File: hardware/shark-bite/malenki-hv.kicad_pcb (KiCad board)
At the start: 2 copper layers, 56.9 x 61.3 mm, 92 parts, among them J1 Conn_01x02_Male-Connector, J2 Conn_01x08_Male, J3 Conn_01x02, J4 Conn_01x02_Male-Connector, J5 Conn_01x02_Male-Connector, J6 Conn_01x03_Pin, U1 GM7333, U10 IRFH7440TRPBF, U11 IRFH7440TRPBF, U12 IRFH7440TRPBF, U13 DRV8231DSGR, U14 DRV8231DSGR, U2 ATTiny1616-MNR, U3 A7105, U4 GD32E230G6U6TR, U5 FD6288Q, U6 AOZ1282CI, U7 IRFH7440TRPBF, U8 IRFH7440TRPBF, U9 IRFH7440TRPBF, Y1 16mhz Seiko Epson Q24FA20H005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

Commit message: Routed Without Debug
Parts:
- moved C20 0.90 mm to (130.2, 76.9)
- moved C3 0.70 mm to (113.1, 52.5)
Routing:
- net GND: track 380.8 -> 368.9 mm, vias 63 -> 57
- net VLOGIC: track 117.7 -> 127.2 mm
- net BEMF_A: track 12.5 -> 16.8 mm
- net TXDEBUG: track 37.2 -> 35.2 mm
- net Net-(U2-PA3): track 14.1 -> 15.8 mm
- net GATE_HIGH_B: track 27.5 -> 29.0 mm
- net OUT_B: track 70.3 -> 71.4 mm
- net OUT_A: track 73.0 -> 74.0 mm
- net VSENSE: track 10.7 -> 11.7 mm
- net GATE_HIGH_A: track 23.9 -> 24.5 mm, vias 5 -> 4
- net Net-(D5-K): track 14.3 -> 14.9 mm
- net GIO1: track 23.3 -> 23.9 mm
- net GATE_LOW_B: track 26.1 -> 26.6 mm

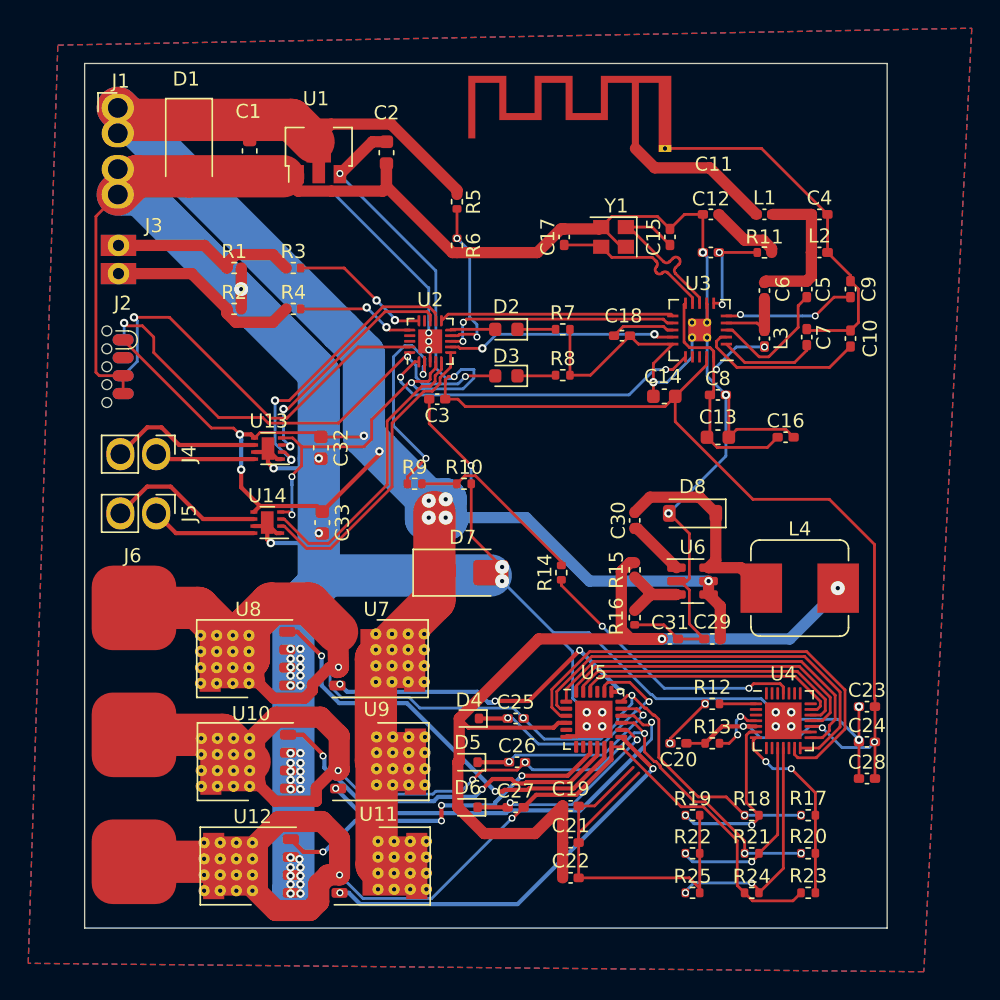
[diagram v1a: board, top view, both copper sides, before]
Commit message: Added Gate Resistors and Power Capacitors
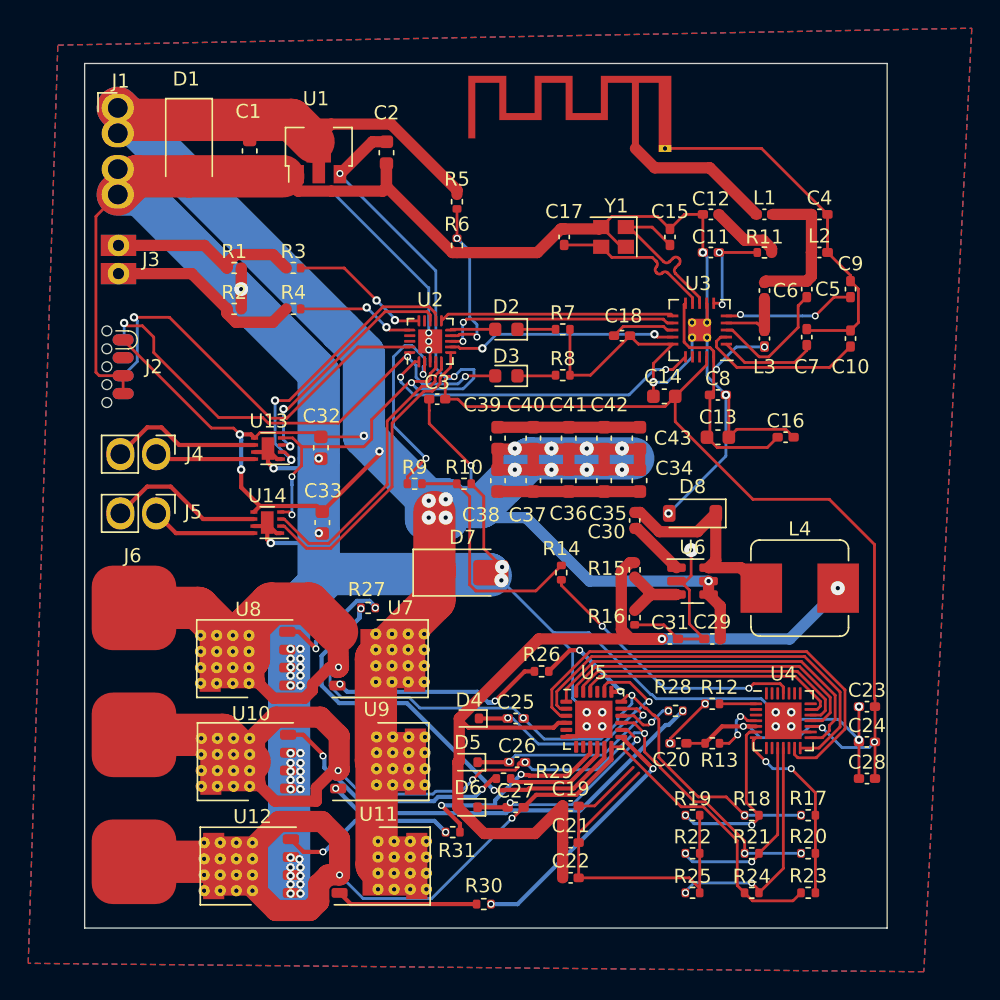
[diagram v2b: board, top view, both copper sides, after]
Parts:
- added C34: 10uF, Capacitor_SMD:C_0603_1608Metric, F.Cu at (127.4, 58.3)
- added C35: 10uF, Capacitor_SMD:C_0603_1608Metric, F.Cu at (124.9, 58.3)
- added C36: 10uF, Capacitor_SMD:C_0603_1608Metric, F.Cu at (122.4, 58.3)
- added C37: 10uF, Capacitor_SMD:C_0603_1608Metric, F.Cu at (119.9, 58.3)
- added C38: 10uF, Capacitor_SMD:C_0603_1608Metric, F.Cu at (117.4, 58.3)
- added C39: 10uF, Capacitor_SMD:C_0603_1608Metric, F.Cu at (117.4, 55.3)
- added C40: 10uF, Capacitor_SMD:C_0603_1608Metric, F.Cu at (119.9, 55.3)
- added C41: 10uF, Capacitor_SMD:C_0603_1608Metric, F.Cu at (122.4, 55.3)
- added C42: 10uF, Capacitor_SMD:C_0603_1608Metric, F.Cu at (124.9, 55.3)
- added C43: 10uF, Capacitor_SMD:C_0603_1608Metric, F.Cu at (127.4, 55.3)
- added R26: 20, Resistor_SMD:R_0402_1005Metric, F.Cu at (120.5, 71.8)
- added R27: 20, Resistor_SMD:R_0402_1005Metric, F.Cu at (108.2, 67.3)
- added R28: 20, Resistor_SMD:R_0402_1005Metric, F.Cu at (130.0, 74.6)
- added R29: 20, Resistor_SMD:R_0402_1005Metric, F.Cu at (117.8, 79.4)
- added R30: 20, Resistor_SMD:R_0402_1005Metric, F.Cu at (116.4, 88.3)
- added R31: 20, Resistor_SMD:R_0402_1005Metric, F.Cu at (114.2, 83.2)
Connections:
- U10 pad 1: GATE_LOW_B -> Net-(U10-G)
- U11 pad 1: GATE_HIGH_C -> Net-(U11-G)
- U12 pad 1: GATE_LOW_C -> Net-(U12-G)
- U7 pad 1: GATE_HIGH_A -> Net-(U7-G)
- U8 pad 1: GATE_LOW_A -> Net-(U8-G)
- U9 pad 1: GATE_HIGH_B -> Net-(U9-G)
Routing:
- net VBAT: track 163.7 -> 206.1 mm, vias 9 -> 17
- net Net-(U9-G): track 0.00 -> 28.3 mm, vias 0 -> 2
- net GATE_HIGH_B: track 29.0 -> 4.02 mm
- net GATE_LOW_B: track 26.6 -> 7.63 mm, vias 2 -> 0
- net Net-(U10-G): track 0.00 -> 17.9 mm, vias 0 -> 2
- net GND: track 368.9 -> 386.2 mm, vias 57 -> 58
- net GATE_HIGH_A: track 24.5 -> 7.58 mm, vias 4 -> 2
- net Net-(U7-G): track 0.00 -> 15.9 mm, vias 0 -> 2
- net Net-(U12-G): track 0.00 -> 12.6 mm, vias 0 -> 2
- net GATE_HIGH_C: track 29.7 -> 18.6 mm
- net GATE_LOW_C: track 25.7 -> 15.4 mm, vias 4 -> 2
- net Net-(U11-G): track 0.00 -> 10.0 mm
- net Net-(U8-G): track 0.00 -> 8.69 mm, vias 0 -> 2
- net MOTOR1: track 12.9 -> 17.4 mm
- net GATE_LOW_A: track 30.2 -> 32.2 mm

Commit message: Minor Changes???
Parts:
- removed AE1: ~, malenki-nano:malenki_antenna
- removed C12: 10nF, Capacitor_SMD:C_0402_1005Metric_Pad0.74x0.62mm_HandSolder
- removed C13, C14: 2.2uF, Capacitor_SMD:C_0603_1608Metric
- removed C15, C17: 10pF, Capacitor_SMD:C_0402_1005Metric_Pad0.74x0.62mm_HandSolder
- removed C16, C18, C19, C30: 100nF, Capacitor_SMD:C_0402_1005Metric_Pad0.74x0.62mm_HandSolder
- removed C24, C25, C26, C27: 1uF, Capacitor_SMD:C_0402_1005Metric_Pad0.74x0.62mm_HandSolder
- removed C29, C31: 10uF, Capacitor_SMD:C_0402_1005Metric_Pad0.74x0.62mm_HandSolder
- removed C32, C33: 10uF 25V, Capacitor_SMD:C_0603_1608Metric
- removed D3: LED Red, LED_SMD:LED_0603_1608Metric
- removed D4, D5, D6: 1N4148WT, Diode_SMD:D_SOD-523
- removed D7: SMAJ18A, Diode_SMD:D_SMA
- removed D8: B5817W, Diode_SMD:D_SOD-123
- removed J4, J5: Conn_01x02_Male-Connector, malenki-nano:PinHeader_1x02_P2.54mm_BIG1
- removed L1: 2.7nH, Inductor_SMD:L_0402_1005Metric_Pad0.77x0.64mm_HandSolder
- removed L2, L3: 4.7nH, Inductor_SMD:L_0402_1005Metric_Pad0.77x0.64mm_HandSolder
- removed L4: 22uH, Inductor_SMD:L_Bourns_SRP7028A_7.3x6.6mm
- removed R1, R10, R2, R6: 10k, Resistor_SMD:R_0402_1005Metric
- removed R11: 200R, Resistor_SMD:R_0402_1005Metric
- removed R15: 49.9K, Resistor_SMD:R_0402_1005Metric
- removed R16: 4.32K, Resistor_SMD:R_0402_1005Metric
- removed R3, R4, R7, R9: 470R, Resistor_SMD:R_0402_1005Metric
- removed R5: 100k, Resistor_SMD:R_0402_1005Metric
- removed R8: 1k, Resistor_SMD:R_0402_1005Metric
- removed U13, U14: DRV8231DSGR, Package_SON:WSON-8-1EP_2x2mm_P0.5mm_EP0.9x1.6mm
- removed U5: FD6288Q, Package_DFN_QFN:QFN-24-1EP_4x4mm_P0.5mm_EP2.65x2.65mm
- removed U6: AOZ1282CI, Package_TO_SOT_SMD:SOT-23-6
- removed Y1: 16mhz Seiko Epson Q24FA20H0051200, Crystal:Crystal_SMD_2520-4Pin_2.5x2.0mm
- added TP1: TestPoint, TestPoint:TestPoint_Pad_1.0x1.0mm, F.Cu at (125.5, 80.7)
- added TP2: TestPoint, TestPoint:TestPoint_Pad_1.0x1.0mm, F.Cu at (114.0, 65.3)
- C1, C2: value 10uF 25V -> 10uF
- C10, C3: value 100nF -> 1uF; footprint Capacitor_SMD:C_0402_1005Metric_Pad0.74x0.62mm_HandSolder -> Capacitor_SMD:C_0603_1608Metric
- C11: value 560pF -> 1uF; footprint Capacitor_SMD:C_0402_1005Metric_Pad0.74x0.62mm_HandSolder -> Capacitor_SMD:C_0603_1608Metric
- C22: value 4.7uF -> 10uF
- C23: value 100nF -> 10nF
- C28: value 4.7uF -> 1uF
- C4: value 1pF -> 1uF; footprint Capacitor_SMD:C_0402_1005Metric_Pad0.74x0.62mm_HandSolder -> Capacitor_SMD:C_0603_1608Metric
- C5: value 22pF -> 1uF; footprint Capacitor_SMD:C_0402_1005Metric_Pad0.74x0.62mm_HandSolder -> Capacitor_SMD:C_0603_1608Metric
- C6: value 10pF -> 330uF; footprint Capacitor_SMD:C_0402_1005Metric_Pad0.74x0.62mm_HandSolder -> Capacitor_SMD:C_0603_1608Metric
- C7, C8, C9: value 100nF -> 1uF; footprint Capacitor_SMD:C_0402_1005Metric_Pad0.74x0.62mm_HandSolder -> Capacitor_SMD:C_0402_1005Metric
- D2: value LED Blue -> SMF5V0A; footprint LED_SMD:LED_0603_1608Metric -> Diode_SMD:D_SMF
- J1: footprint malenki-nano:malenkipower -> Sharkbite:Power Input
- J2: value Conn_01x08_Male -> Conn_ARM_SWD_TagConnect_TC2030-NL; footprint malenki-nano:SOIC_clipProgSmall -> Connector:Tag-Connect_TC2030-IDC-NL_2x03_P1.27mm_Vertical
- J3: value Conn_01x02 -> PWM Pads; footprint malenki-nano:wirepad_2 -> Connector_PinHeader_1.00mm:PinHeader_1x02_P1.00mm_Vertical
- J6: value Conn_01x03_Pin -> Motor Pads
- R14: value 1K -> 100
- R26, R27, R28, R29, R30, R31: value 20 -> 2.2; footprint Resistor_SMD:R_0402_1005Metric -> Resistor_SMD:R_0603_1608Metric
- U10, U11, U12, U7, U8, U9: value IRFH7440TRPBF -> SISS54; footprint Sharkbite:PQFN FET -> Sharkbite:1212-8S
- U2: value ATTiny1616-MNR -> DRV8300DRGER; footprint Package_DFN_QFN:VQFN-20-1EP_3x3mm_P0.4mm_EP1.7x1.7mm -> Sharkbite:RGE0024B-IPC_A
- U3: value A7105 -> ~; footprint malenki-nano:a7105-QFN-20 -> Package_TO_SOT_SMD:SOT-89-3
- moved C4 56.9 mm to (111.5, 88.5), turned to 180 degrees
- moved C9 55.1 mm to (103.5, 83.8), turned to 0 degrees
- moved C5 53.1 mm to (108.5, 88.0), turned to 180 degrees
- moved J2 49.0 mm to (125.5, 85.5)
- moved J1 48.4 mm to (126.2, 66.3)
- moved J3 48.2 mm to (126.0, 75.2), turned to 180 degrees
- moved C10 45.7 mm to (120.0, 88.0), turned to 0 degrees
- moved C7 44.3 mm to (103.5, 74.2), turned to 0 degrees
- moved C2 44.2 mm to (120.0, 78.0), turned to 0 degrees
- moved U1 42.9 mm to (120.5, 74.5), turned to 0 degrees
- moved C11 40.9 mm to (120.0, 81.0)
- moved C1 40.2 mm to (117.5, 71.0), turned to 180 degrees
- moved D1 39.7 mm to (120.0, 66.0), turned to 180 degrees
- moved R20 38.8 mm to (103.0, 71.2)
- moved U3 38.4 mm to (121.0, 84.5), turned to 0 degrees
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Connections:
- net BEMF_A renamed /motor_driver_1_weapon/BEMF_A
- net BEMF_B renamed /motor_driver_1_weapon/BEMF_B
- net BEMF_C renamed /motor_driver_1_weapon/BEMF_C
- net BEMF_COMMON renamed /motor_driver_1_weapon/BEMF_COM
- C1 pad 1: VBAT -> VBUS
- C10 pad 1: Net-(U3-BPBG) -> +10V
- C11 pad 1: GND -> VBUS
- C11 pad 2: Net-(U3-VT) -> GND
- C2 pad 1: VLOGIC -> +3V3
- C20 pad 1: VLOGIC -> +3V3
- C23 pad 2: VLOGIC -> +3V3
- C28 pad 2: VLOGIC -> +3V3
- C3 pad 1: VLOGIC -> Net-(U2-BSTA)
- C3 pad 2: GND -> Net-(U2-SHA)
- C34 pad 1: VBAT -> VBUS
- C35 pad 1: VBAT -> VBUS
- C36 pad 1: VBAT -> VBUS
- C37 pad 1: VBAT -> VBUS
- C38 pad 1: VBAT -> VBUS
- C39 pad 1: VBAT -> VBUS
- C4 pad 1: /radio/IMPMATCH -> Net-(U2-BSTB)
- C4 pad 2: GND -> Net-(U2-SHB)
- C40 pad 1: VBAT -> VBUS
- C41 pad 1: VBAT -> VBUS
- C42 pad 1: VBAT -> VBUS
- C43 pad 1: VBAT -> VBUS
- C5 pad 1: /radio/IMPMATCH -> Net-(U2-BSTC)
- C5 pad 2: /radio/RFI -> Net-(U2-SHC)
- C6 pad 1: /radio/IMPMATCH -> VBUS
- C6 pad 2: /radio/RFO -> GND
- C7 pad 1: Net-(U3-RSSI) -> VBUS
- C8 pad 1: /radio/REGOA -> VBUS
- C9 pad 1: /radio/VDA2 -> VBUS
- D1 pad 1: VBAT -> VBUS
- D2 pad 1: Net-(D2-K) -> /motor_driver_1_weapon/PWM
- D2 pad 2: BLINKY -> GND
- J1 pad 1: VBAT -> VBUS
- J2 pad 1: VBAT -> +3V3
- J2 pad 2: unconnected-(J2-Pin_2-Pad2) -> /motor_driver_1_weapon/SWDIO
- J2 pad 3: GND -> /motor_driver_1_weapon/RST
- J2 pad 4: GND -> /motor_driver_1_weapon/SWDCLK
- J2 pad 5: unconnected-(J2-Pin_5-Pad5) -> GND
- J2 pad 6: UPDI -> unconnected-(J2-SWO-Pad6)
- J3 pad 1: WEAPON3 -> GND
- J3 pad 2: WEAPON2 -> /motor_driver_1_weapon/PWM
- J6 pad 1: OUT_C -> /motor_driver_1_weapon/OUT_C
- J6 pad 2: OUT_B -> /motor_driver_1_weapon/OUT_B
- J6 pad 3: OUT_A -> /motor_driver_1_weapon/OUT_A
- R13 pad 1: VLOGIC -> +3V3
- R13 pad 2: Net-(U4-NRST) -> /motor_driver_1_weapon/RST
- R14 pad 2: MOTOR1 -> /motor_driver_1_weapon/PWM
- R17 pad 2: OUT_A -> /motor_driver_1_weapon/OUT_A
- R18 pad 1: OUT_A -> /motor_driver_1_weapon/OUT_A
- R20 pad 2: OUT_B -> /motor_driver_1_weapon/OUT_B
- R21 pad 1: OUT_B -> /motor_driver_1_weapon/OUT_B
- R23 pad 2: OUT_C -> /motor_driver_1_weapon/OUT_C
- R24 pad 1: OUT_C -> /motor_driver_1_weapon/OUT_C
- R26 pad 1: GATE_HIGH_A -> /motor_driver_1_weapon/GHA
- R27 pad 1: GATE_LOW_A -> /motor_driver_1_weapon/GLA
- R28 pad 2: GATE_HIGH_B -> /motor_driver_1_weapon/GHB
- R29 pad 1: GATE_LOW_B -> /motor_driver_1_weapon/GLB
- R30 pad 2: GATE_HIGH_C -> /motor_driver_1_weapon/GHC
- R31 pad 2: GATE_LOW_C -> /motor_driver_1_weapon/GLC
- U1 pad 2: VBAT -> VBUS
- U1 pad 3: VLOGIC -> +3V3
- U2 pad 1: GIO1 -> /motor_driver_1_weapon/ALOW
- U2 pad 10: BLINKY -> /motor_driver_1_weapon/GLB
- U2 pad 11: SPI_SCS -> /motor_driver_1_weapon/GLA
- U2 pad 12: MOTOR2F -> Net-(U2-SHC)
- U2 pad 13: MOTOR2R -> /motor_driver_1_weapon/GHC
- U2 pad 14: unconnected-(U2-PB0-Pad14) -> Net-(U2-BSTC)
- U2 pad 15: /W2 -> Net-(U2-SHB)
- U2 pad 16: /W3 -> /motor_driver_1_weapon/GHB
- U2 pad 17: unconnected-(U2-PC2-Pad17) -> Net-(U2-BSTB)
- U2 pad 18: unconnected-(U2-PC3-Pad18) -> Net-(U2-SHA)
- U2 pad 19: UPDI -> /motor_driver_1_weapon/GHA
- U2 pad 2: Net-(U2-PA3) -> /motor_driver_1_weapon/BLOW
- U2 pad 20: TXDEBUG -> Net-(U2-BSTA)
- U2 pad 21: GND -> Net-(U2-DT)
- U2 pad 3: GND -> /motor_driver_1_weapon/CLOW
- U2 pad 4: VLOGIC -> +10V
- U2 pad 5: MOTOR3R -> Net-(U2-MODE)
- U2 pad 6: MOTOR3F -> GND
- U2 pad 7: SPI_SDIO -> unconnected-(U2-NC-Pad7)
- U2 pad 8: SPI_SCK -> unconnected-(U2-NC-Pad8)
- U2 pad 9: VSENSE -> /motor_driver_1_weapon/GLC
- U3 pad 1: Net-(U3-RSSI) -> GND
- U3 pad 2: Net-(U3-BPBG) -> VBUS
- U3 pad 3: /radio/RFI -> +10V
- U4 pad 13: CLOW -> /motor_driver_1_weapon/CLOW
- U4 pad 14: BLOW -> /motor_driver_1_weapon/BLOW
- U4 pad 15: ALOW -> /motor_driver_1_weapon/ALOW
- U4 pad 17: VLOGIC -> +3V3
- U4 pad 18: CHIGH -> /motor_driver_1_weapon/CHIGH
- U4 pad 19: BHIGH -> /motor_driver_1_weapon/BHIGH
- U4 pad 20: AHIGH -> /motor_driver_1_weapon/AHIGH
- U4 pad 21: SWDIO -> /motor_driver_1_weapon/SWDIO
- U4 pad 22: SWDCLK -> /motor_driver_1_weapon/SWDCLK
- U4 pad 4: Net-(U4-NRST) -> /motor_driver_1_weapon/RST
- U4 pad 5: VLOGIC -> +3V3
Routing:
- net GND: track 386.2 -> 21.7 mm, vias 58 -> 122
- net VBAT: track 206.1 -> 0.00 mm, vias 17 -> 0
- net VLOGIC: track 127.2 -> 0.00 mm, vias 8 -> 0
- net OUT_A: track 74.0 -> 0.00 mm, vias 5 -> 0
- net OUT_C: track 73.8 -> 0.00 mm, vias 2 -> 0
- net OUT_B: track 71.6 -> 0.00 mm, vias 6 -> 0
- net +10V: track 67.8 -> 15.8 mm, vias 2 -> 8
- net Net-(U2-MODE): track 0.00 -> 41.6 mm, vias 0 -> 4
- net TXDEBUG: track 35.2 -> 0.00 mm, vias 3 -> 0
- net CLOW: track 33.3 -> 0.00 mm
- net /motor_driver_1_weapon/RST: track 0.00 -> 33.2 mm, vias 0 -> 2
- net GATE_LOW_A: track 32.2 -> 0.00 mm, vias 2 -> 0
- net BLOW: track 29.8 -> 0.00 mm
- net UPDI: track 29.2 -> 0.00 mm, vias 1 -> 0
- net /motor_driver_1_weapon/GHA: track 0.00 -> 27.5 mm, vias 0 -> 2
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- added copper zone on B.Cu, net +10V
- added copper zone on B.Cu, net +3V3
- added copper zone on F.Cu, net /motor_driver_1_weapon/OUT_A
- added copper zone on F.Cu, net /motor_driver_1_weapon/OUT_B
- added copper zone on F.Cu, net /motor_driver_1_weapon/OUT_C
- added copper zone on In1.Cu, net GND
- added copper zone on In2.Cu, net GND
- added copper zone on B.Cu, net VBUS
- added copper zone on F.Cu, net VBUS
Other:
- board size 56.9 x 61.3 mm -> 40 x 26 mm
- copper layers 2 -> 4

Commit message: Design Finished
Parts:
- added G***: LOGO, Sharkbite:Logo1 8x8, B.Cu at (106.7, 75.9)
- U3: value ~ -> 78L10
- moved C7 3.37 mm to (101.7, 77.1), turned to -90 degrees
- moved C8 3.37 mm to (101.7, 68.1), turned to -90 degrees
- moved C9 3.29 mm to (101.7, 86.5), turned to -90 degrees
- moved R29 0.45 mm to (103.7, 77.6)
- moved R26 0.20 mm to (103.7, 67.0)
- moved R27 0.20 mm to (103.7, 69.0)
- moved R28 0.20 mm to (103.7, 76.0)
- moved R30 0.20 mm to (103.7, 85.5)
- moved R31 0.20 mm to (103.7, 87.5)
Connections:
- U3 pad 1: GND -> +10V
- U3 pad 2: VBUS -> GND
- U3 pad 3: +10V -> VBUS
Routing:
- net VBUS: track 4.32 -> 5.42 mm, vias 105 -> 104
- net Net-(U11-G): track 6.78 -> 5.81 mm, vias 0 -> 2
- net +10V: track 15.8 -> 16.7 mm, vias 8 -> 7
- net /motor_driver_1_weapon/BEMF_B: track 15.7 -> 16.5 mm
- net Net-(U9-G): track 6.37 -> 5.82 mm, vias 0 -> 2
- net Net-(U12-G): track 2.44 -> 2.69 mm, vias 0 -> 2
- net Net-(U8-G): track 2.37 -> 2.62 mm, vias 0 -> 2
- net Net-(U7-G): track 6.13 -> 5.90 mm, vias 0 -> 2
- net Net-(U10-G): track 2.38 -> 2.52 mm, vias 0 -> 2
- net GND: vias 122 -> 120
- added copper zone on In2.Cu, net +10V
- added copper zone on In2.Cu, net +3V3
- added copper zone on In2.Cu, net VBUS
- removed copper zone on B.Cu, net +10V
- removed copper zone on B.Cu, net +3V3
- removed copper zone on B.Cu, net VBUS
